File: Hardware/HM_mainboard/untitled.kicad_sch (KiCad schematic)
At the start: 13 parts, among them J1 JST PH2P ST90, Q1 PMOS AS3401, U1 MCP73831-2, U2 TC1262-33

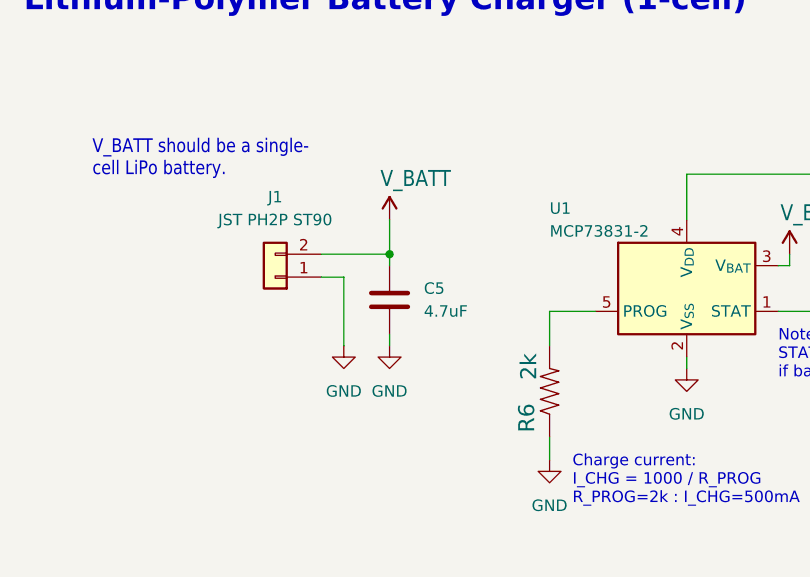
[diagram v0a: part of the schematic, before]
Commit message: Swapped battery polarity due to wrong pinning assumption
Bugfix
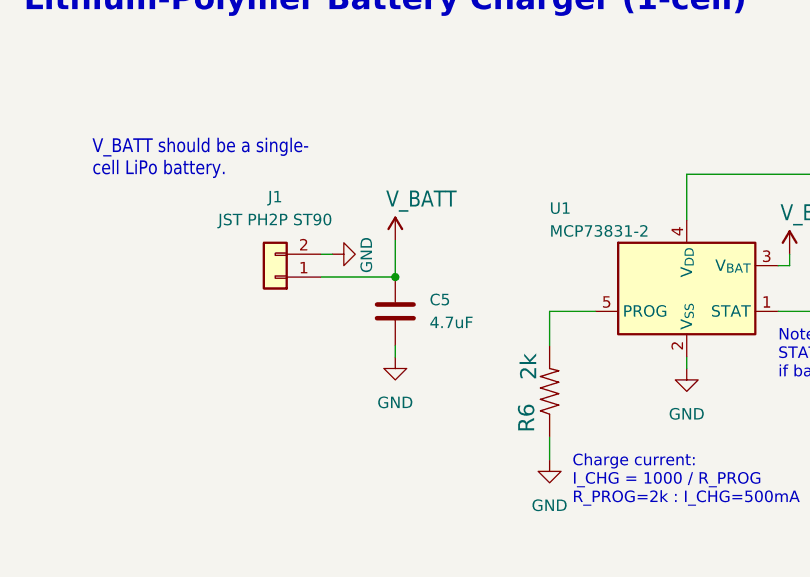
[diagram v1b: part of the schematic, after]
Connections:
- net GND: now also J1.2 (Pin_2); no longer J1.1 (Pin_1)
- net V_BATT: now also J1.1 (Pin_1); no longer J1.2 (Pin_2)
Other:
- moved on the sheet: C5
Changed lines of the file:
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@@
   (junction (at 56.515 59.055) (diameter 0) (color 0 0 0 0)
   )
+  (junction (at 65.405 146.05) (diameter 0) (color 0 0 0 0)
+  )
   (junction (at 200.66 138.43) (diameter 0) (color 0 0 0 0)
   )
@@
   (junction (at 46.355 51.435) (diameter 0) (color 0 0 0 0)
   )
-  (junction (at 64.77 143.51) (diameter 0) (color 0 0 0 0)
-  )
   (wire (pts (xy 97.79 156.21) (xy 97.79 154.94))
     (stroke (width 0) (type default))
@@
     (stroke (width 0) (type default))
   )
+  (wire (pts (xy 65.405 141.986) (xy 65.405 146.05))
+    (stroke (width 0.1524) (type solid))
+  )
   (wire (pts (xy 200.66 138.43) (xy 200.66 140.97))
     (stroke (width 0) (type default))
   )
-  (wire (pts (xy 64.77 153.67) (xy 64.77 152.4))
+  (wire (pts (xy 65.405 154.94) (xy 65.405 153.67))
     (stroke (width 0) (type default))
   )
@@
     (stroke (width 0) (type default))
   )
-  (wire (pts (xy 57.15 146.05) (xy 59.69 146.05))
-    (stroke (width 0.1524) (type solid))
+  (wire (pts (xy 57.15 146.05) (xy 65.405 146.05))
+    (stroke (width 0) (type default))
   )
   (wire (pts (xy 104.775 59.055) (xy 112.395 59.055))
@@
     (stroke (width 0.1524) (type solid))
   )
-  (wire (pts (xy 57.15 143.51) (xy 64.77 143.51))
-    (stroke (width 0.1524) (type solid))
-  )
   (wire (pts (xy 41.275 66.675) (xy 41.275 64.135))
     (stroke (width 0.1524) (type solid))
   )
-  (wire (pts (xy 64.77 143.51) (xy 64.77 144.78))
-    (stroke (width 0.1524) (type solid))
-  )
   (wire (pts (xy 82.55 149.86) (xy 87.63 149.86))
     (stroke (width 0.1524) (type solid))
@@
     (stroke (width 0.1524) (type solid))
   )
-  (wire (pts (xy 64.77 143.51) (xy 64.77 139.7))
-    (stroke (width 0.1524) (type solid))
-  )
   (wire (pts (xy 200.66 153.67) (xy 200.66 151.13))
     (stroke (width 0) (type default))
@@
     (stroke (width 0) (type default))
   )
-  (wire (pts (xy 59.69 146.05) (xy 59.69 153.67))
-    (stroke (width 0.1524) (type solid))
-  )
   (wire (pts (xy 41.275 53.975) (xy 41.275 51.435))
     (stroke (width 0.1524) (type solid))
@@
   )
   (wire (pts (xy 132.715 59.055) (xy 137.795 59.055))
+    (stroke (width 0.1524) (type solid))
+  )
+  (wire (pts (xy 58.42 143.51) (xy 57.15 143.51))
     (stroke (width 0.1524) (type solid))
   )
@@
     )
   )
-  (symbol (lib_id "Device:C") (at 64.77 148.59 0) (unit 1)
-    (in_bom yes) (on_board yes) (dnp no) (fields_autoplaced)
-    (property "Reference" "C5" (at 68.58 147.32 0)
+  (symbol (lib_id "Device:C") (at 65.405 149.86 0) (unit 1)
+    (in_bom yes) (on_board yes) (dnp no) (fields_autoplaced)
+    (property "Reference" "C5" (at 69.215 148.59 0)
       (effects (font (size 1.27 1.27)) (justify left))
     )
-    (property "Value" "4.7uF" (at 68.58 149.86 0)
+    (property "Value" "4.7uF" (at 69.215 151.13 0)
       (effects (font (size 1.27 1.27)) (justify left))
     )
-    (property "Footprint" "Capacitor_SMD:C_0603_1608Metric_Pad1.08x0.95mm_HandSolder" (at 65.7352 152.4 0)
-      (effects (font (size 1.27 1.27)) hide)
-    )
-    (property "Datasheet" "~" (at 64.77 148.59 0)
-      (effects (font (size 1.27 1.27)) hide)
-    )
-    (property "Reichelt" "" (at 64.77 148.59 0)
+    (property "Footprint" "Capacitor_SMD:C_0603_1608Metric_Pad1.08x0.95mm_HandSolder" (at 66.3702 153.67 0)
+      (effects (font (size 1.27 1.27)) hide)
+    )
+    (property "Datasheet" "~" (at 65.405 149.86 0)
+      (effects (font (size 1.27 1.27)) hide)
+    )
+    (property "Reichelt" "" (at 65.405 149.86 0)
       (effects (font (size 1.27 1.27)) hide)
     )
@@
     )
   )
-  (symbol (lib_name "GND_1") (lib_id "power:GND") (at 59.69 153.67 0) (unit 1)
-    (in_bom yes) (on_board yes) (dnp no) (fields_autoplaced)
-    (property "Reference" "#PWR06" (at 59.69 160.02 0)
-      (effects (font (size 1.27 1.27)) hide)
-    )
-    (property "Value" "GND" (at 59.69 158.75 0)
-      (effects (font (size 1.27 1.27)))
-    )
-    (property "Footprint" "" (at 59.69 153.67 0)
-      (effects (font (size 1.27 1.27)) hide)
-    )
-    (property "Datasheet" "" (at 59.69 153.67 0)
+  (symbol (lib_name "GND_1") (lib_id "power:GND") (at 58.42 143.51 90) (unit 1)
+    (in_bom yes) (on_board yes) (dnp no)
+    (property "Reference" "#PWR06" (at 64.77 143.51 0)
+      (effects (font (size 1.27 1.27)) hide)
+    )
+    (property "Value" "GND" (at 62.23 141.605 0)
+      (effects (font (size 1.27 1.27)) (justify right))
+    )
+    (property "Footprint" "" (at 58.42 143.51 0)
+      (effects (font (size 1.27 1.27)) hide)
+    )
+    (property "Datasheet" "" (at 58.42 143.51 0)
       (effects (font (size 1.27 1.27)) hide)
     )
@@
     )
   )
-  (symbol (lib_name "GND_1") (lib_id "power:GND") (at 64.77 153.67 0) (unit 1)
-    (in_bom yes) (on_board yes) (dnp no) (fields_autoplaced)
-    (property "Reference" "#PWR06" (at 64.77 160.02 0)
-      (effects (font (size 1.27 1.27)) hide)
-    )
-    (property "Value" "GND" (at 64.77 158.75 0)
+  (symbol (lib_name "GND_1") (lib_id "power:GND") (at 65.405 154.94 0) (unit 1)
+    (in_bom yes) (on_board yes) (dnp no) (fields_autoplaced)
+    (property "Reference" "#PWR06" (at 65.405 161.29 0)
+      (effects (font (size 1.27 1.27)) hide)
+    )
+    (property "Value" "GND" (at 65.405 160.02 0)
       (effects (font (size 1.27 1.27)))
     )
-    (property "Footprint" "" (at 64.77 153.67 0)
-      (effects (font (size 1.27 1.27)) hide)
-    )
-    (property "Datasheet" "" (at 64.77 153.67 0)
+    (property "Footprint" "" (at 65.405 154.94 0)
+      (effects (font (size 1.27 1.27)) hide)
+    )
+    (property "Datasheet" "" (at 65.405 154.94 0)
       (effects (font (size 1.27 1.27)) hide)
     )
@@
     )
   )
-  (symbol (lib_id "esp32-thing-eagle-import:V_BATT") (at 64.77 139.7 0) (unit 1)
-    (in_bom yes) (on_board yes) (dnp no)
-    (property "Reference" "#SUPPLY05" (at 64.77 139.7 0)
-      (effects (font (size 1.27 1.27)) hide)
-    )
-    (property "Value" "V_BATT" (at 63.754 136.144 0)
+  (symbol (lib_id "esp32-thing-eagle-import:V_BATT") (at 65.405 141.986 0) (unit 1)
+    (in_bom yes) (on_board yes) (dnp no)
+    (property "Reference" "#SUPPLY05" (at 65.405 141.986 0)
+      (effects (font (size 1.27 1.27)) hide)
+    )
+    (property "Value" "V_BATT" (at 64.389 138.43 0)
       (effects (font (size 1.778 1.5113)) (justify left bottom))
     )
-    (property "Footprint" "" (at 64.77 139.7 0)
-      (effects (font (size 1.27 1.27)) hide)
-    )
-    (property "Datasheet" "" (at 64.77 139.7 0)
-      (effects (font (size 1.27 1.27)) hide)
-    )
+    (property "Footprint" "" (at 65.405 141.986 0)
+      (effects (font (size 1.27 1.27)) hide)
+    )
+    (property "Datasheet" "" (at 65.405 141.986 0)
+      (effects (font (size 1.27 1.27)) hide)
+    )
